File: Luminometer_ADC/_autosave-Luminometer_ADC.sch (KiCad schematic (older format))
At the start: 69 parts, among them J1 Harting__15210122401000, U1 LT3464, U2 ADA4522-1, U3 ADR512, U4 ADR512, U5 ADA4522-4, U6 LP5907MFX-3, U7 ADS131M08IPBS

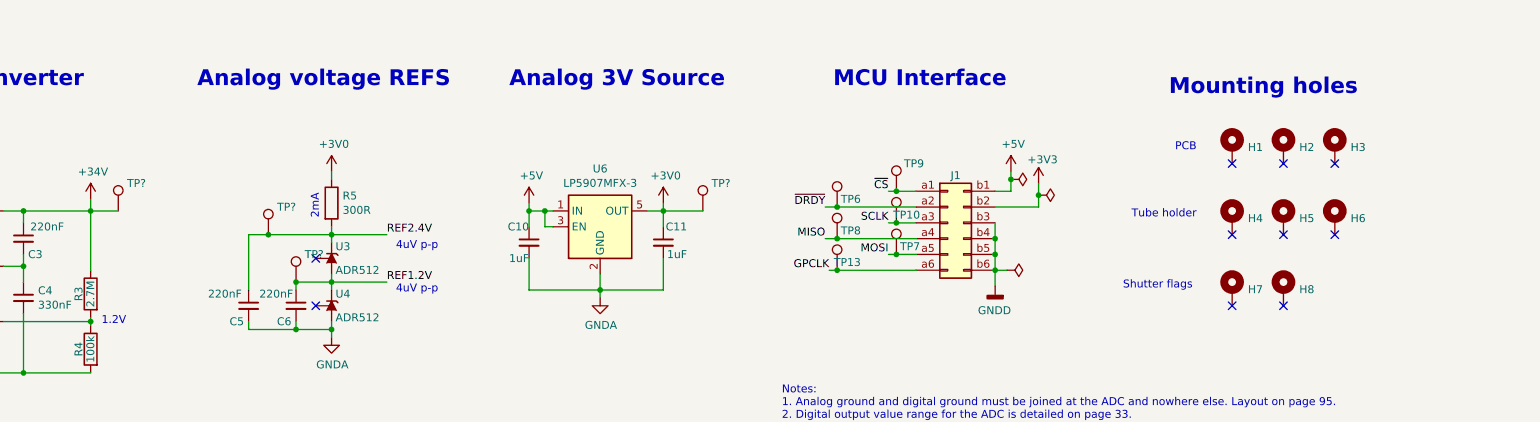
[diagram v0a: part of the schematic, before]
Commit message: Changes to design
- Standardized mounting hole pattern to match Pi zero.
- Rounded corners to 3 mm
- Moved all test points to back side of board.
- Added test points for +34V, 1.2V, 2.4V
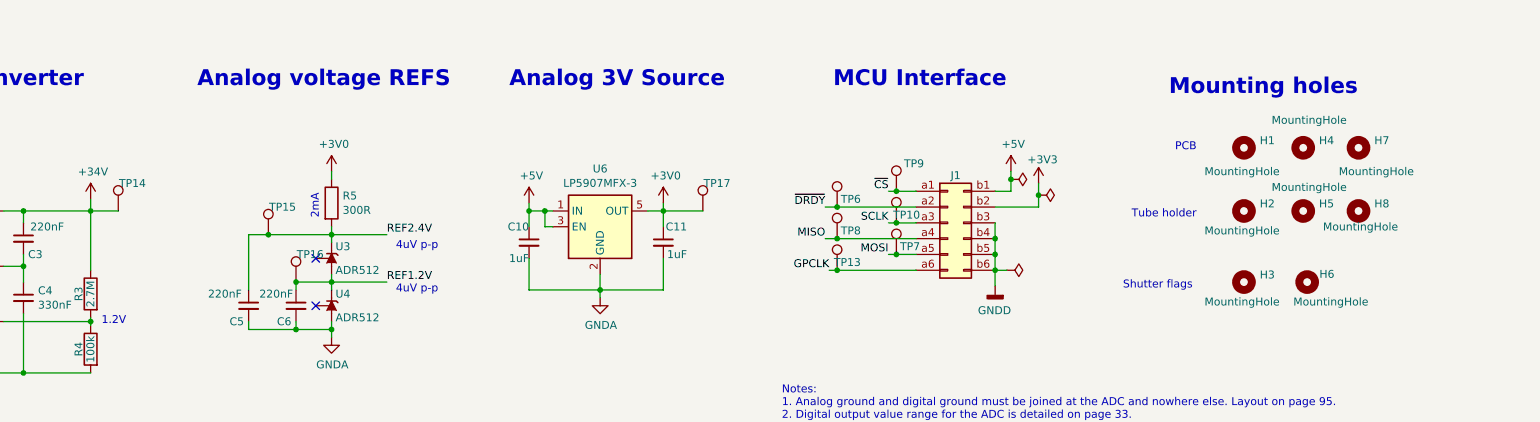
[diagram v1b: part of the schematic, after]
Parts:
- removed H1, H2, H3: MountingHole_Pad, MountingHole:MountingHole_2.7mm_M2.5_DIN965_Pad, symbol Mechanical:MountingHole_Pad
- removed H4, H5, H6: MountingHole_Pad, MountingHole:MountingHole_2.5mm, symbol Mechanical:MountingHole_Pad
- removed H7, H8: MountingHole_Pad, MountingHole:MountingHole_2.2mm_M2, symbol Mechanical:MountingHole_Pad
- added H1, H2, H4, H5, H7, H8: MountingHole, MountingHole:MountingHole_2.7mm_M2.5, symbol Mechanical:MountingHole
- added H3, H6: MountingHole, MountingHole:MountingHole_2.2mm_M2, symbol Mechanical:MountingHole
- gave numbers to parts that had none: 4
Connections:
- no-connect marks 13 -> 5
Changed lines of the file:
@@
 Connection ~ 10575 3050
-$Comp
-L Mechanical:MountingHole_Pad H1
-U 1 1 5F30D92E
-P 9850 5075
-F 0 "H1" H 9950 5078 50  0000 L CNN
-F 1 "MountingHole_Pad" H 9950 5033 50  0001 L CNN
-F 2 "MountingHole:MountingHole_2.7mm_M2.5_DIN965_Pad" H 9850 5075 50  0001 C CNN
-F 3 "~" H 9850 5075 50  0001 C CNN
-	1    9850 5075
-	1    0    0    -1
-$EndComp
 $Comp
 L LuminometerCustomPartLib:MICROFC−60035−SMT SiPM1
@@
 Wire Wire Line
 	3800 3325 3800 3375
-$Comp
-L Mechanical:MountingHole_Pad H2
-U 1 1 6163C291
-P 10175 5075
-F 0 "H2" H 10275 5078 50  0000 L CNN
-F 1 "MountingHole_Pad" H 10275 5033 50  0001 L CNN
-F 2 "MountingHole:MountingHole_2.7mm_M2.5_DIN965_Pad" H 10175 5075 50  0001 C CNN
-F 3 "~" H 10175 5075 50  0001 C CNN
-	1    10175 5075
-	1    0    0    -1
-$EndComp
-$Comp
-L Mechanical:MountingHole_Pad H3
-U 1 1 6163C601
-P 10500 5075
-F 0 "H3" H 10600 5078 50  0000 L CNN
-F 1 "MountingHole_Pad" H 10600 5033 50  0001 L CNN
-F 2 "MountingHole:MountingHole_2.7mm_M2.5_DIN965_Pad" H 10500 5075 50  0001 C CNN
-F 3 "~" H 10500 5075 50  0001 C CNN
-	1    10500 5075
-	1    0    0    -1
-$EndComp
-NoConn ~ 10500 5175
-NoConn ~ 10175 5175
-NoConn ~ 9850 5175
 Text Notes 5675 1900 0    39   ~ 0
 Precision
@@
 $EndComp
 Connection ~ 10575 3550
-$Comp
-L Mechanical:MountingHole_Pad H4
-U 1 1 616FF489
-P 9850 5525
-F 0 "H4" H 9950 5528 50  0000 L CNN
-F 1 "MountingHole_Pad" H 9950 5483 50  0001 L CNN
-F 2 "MountingHole:MountingHole_2.5mm" H 9850 5525 50  0001 C CNN
-F 3 "~" H 9850 5525 50  0001 C CNN
-	1    9850 5525
-	1    0    0    -1
-$EndComp
 Text Notes 9625 5100 2    50   ~ 0
 PCB
 Text Notes 9625 5525 2    50   ~ 0
 Tube holder
-$Comp
-L Mechanical:MountingHole_Pad H5
-U 1 1 61761F5F
-P 10175 5525
-F 0 "H5" H 10275 5528 50  0000 L CNN
-F 1 "MountingHole_Pad" H 10275 5483 50  0001 L CNN
-F 2 "MountingHole:MountingHole_2.5mm" H 10175 5525 50  0001 C CNN
-F 3 "~" H 10175 5525 50  0001 C CNN
-	1    10175 5525
-	1    0    0    -1
-$EndComp
-$Comp
-L Mechanical:MountingHole_Pad H6
-U 1 1 617622BC
-P 10500 5525
-F 0 "H6" H 10600 5528 50  0000 L CNN
-F 1 "MountingHole_Pad" H 10600 5483 50  0001 L CNN
-F 2 "MountingHole:MountingHole_2.5mm" H 10500 5525 50  0001 C CNN
-F 3 "~" H 10500 5525 50  0001 C CNN
-	1    10500 5525
-	1    0    0    -1
-$EndComp
-$Comp
-L Mechanical:MountingHole_Pad H7
-U 1 1 61762E6B
-P 9850 5975
-F 0 "H7" H 9950 5978 50  0000 L CNN
-F 1 "MountingHole_Pad" H 9950 5933 50  0001 L CNN
-F 2 "MountingHole:MountingHole_2.2mm_M2" H 9850 5975 50  0001 C CNN
-F 3 "~" H 9850 5975 50  0001 C CNN
-	1    9850 5975
-	1    0    0    -1
-$EndComp
-$Comp
-L Mechanical:MountingHole_Pad H8
-U 1 1 617631A2
-P 10175 5975
-F 0 "H8" H 10275 5978 50  0000 L CNN
-F 1 "MountingHole_Pad" H 10275 5933 50  0001 L CNN
-F 2 "MountingHole:MountingHole_2.2mm_M2" H 10175 5975 50  0001 C CNN
-F 3 "~" H 10175 5975 50  0001 C CNN
-	1    10175 5975
-	1    0    0    -1
-$EndComp
 Text Notes 9600 5975 2    50   ~ 0
 Shutter flags
@@
 Wire Wire Line
 	3625 5625 3750 5625
-NoConn ~ 9850 5625
-NoConn ~ 10175 5625
-NoConn ~ 10500 5625
-NoConn ~ 9850 6075
-NoConn ~ 10175 6075
-$Comp
-L Connector:TestPoint TP?
+$Comp
+L Connector:TestPoint TP17
 U 1 1 5FD30742
 P 6500 5475
-F 0 "TP?" H 6675 5650 50  0000 R CNN
+F 0 "TP17" H 6675 5650 50  0000 R CNN
 F 1 "TestPoint" H 6600 5675 50  0001 R CNN
 F 2 "TestPoint:TestPoint_Pad_D1.5mm" H 6700 5475 50  0001 C CNN
@@
 	6500 5475 6250 5475
 $Comp
-L Connector:TestPoint TP?
+L Connector:TestPoint TP15
 U 1 1 5FD40634
 P 3750 5625
-F 0 "TP?" H 3925 5800 50  0000 R CNN
+F 0 "TP15" H 3925 5800 50  0000 R CNN
 F 1 "TestPoint" H 3850 5825 50  0001 R CNN
 F 2 "TestPoint:TestPoint_Pad_D1.5mm" H 3950 5625 50  0001 C CNN
@@
 	3750 5625 4150 5625
 $Comp
-L Connector:TestPoint TP?
+L Connector:TestPoint TP16
 U 1 1 5FD40C16
 P 3925 5925
-F 0 "TP?" H 4100 6100 50  0000 R CNN
+F 0 "TP16" H 4100 6100 50  0000 R CNN
 F 1 "TestPoint" H 4025 6125 50  0001 R CNN
 F 2 "TestPoint:TestPoint_Pad_D1.5mm" H 4125 5925 50  0001 C CNN
@@
 Connection ~ 3925 5925
 $Comp
-L Connector:TestPoint TP?
+L Connector:TestPoint TP14
 U 1 1 5FD40E56
 P 2800 5475
-F 0 "TP?" H 2975 5650 50  0000 R CNN
+F 0 "TP14" H 2975 5650 50  0000 R CNN
 F 1 "TestPoint" H 2900 5675 50  0001 R CNN
 F 2 "TestPoint:TestPoint_Pad_D1.5mm" H 3000 5475 50  0001 C CNN
@@
 Wire Wire Line
 	2800 5475 2625 5475
+$Comp
+L Mechanical:MountingHole H3
+U 1 1 5FD63B89
+P 9925 5925
+F 0 "H3" H 10025 5971 50  0000 L CNN
+F 1 "MountingHole" H 9675 5800 50  0000 L CNN
+F 2 "MountingHole:MountingHole_2.2mm_M2" H 9925 5925 50  0001 C CNN
+F 3 "~" H 9925 5925 50  0001 C CNN
+	1    9925 5925
+	1    0    0    -1
+$EndComp
+$Comp
+L Mechanical:MountingHole H6
+U 1 1 5FDB2C55
+P 10325 5925
+F 0 "H6" H 10450 5975 50  0000 C CNN
+F 1 "MountingHole" H 10475 5800 50  0000 C CNN
+F 2 "MountingHole:MountingHole_2.2mm_M2" H 10325 5925 50  0001 C CNN
+F 3 "~" H 10325 5925 50  0001 C CNN
+	1    10325 5925
+	1    0    0    -1
+$EndComp
+$Comp
+L Mechanical:MountingHole H2
+U 1 1 5FD83D7B
+P 9925 5475
+F 0 "H2" H 10025 5521 50  0000 L CNN
+F 1 "MountingHole" H 9675 5350 50  0000 L CNN
+F 2 "MountingHole:MountingHole_2.7mm_M2.5" H 9925 5475 50  0001 C CNN
+F 3 "~" H 9925 5475 50  0001 C CNN
+	1    9925 5475
+	1    0    0    -1
+$EndComp
+$Comp
+L Mechanical:MountingHole H5
+U 1 1 5FD83D85
+P 10300 5475
+F 0 "H5" H 10400 5521 50  0000 L CNN
+F 1 "MountingHole" H 10100 5625 50  0000 L CNN
+F 2 "MountingHole:MountingHole_2.7mm_M2.5" H 10300 5475 50  0001 C CNN
+F 3 "~" H 10300 5475 50  0001 C CNN
+	1    10300 5475
+	1    0    0    -1
+$EndComp
+$Comp
+L Mechanical:MountingHole H8
+U 1 1 5FDB2488
+P 10650 5475
+F 0 "H8" H 10750 5521 50  0000 L CNN
+F 1 "MountingHole" H 10425 5375 50  0000 L CNN
+F 2 "MountingHole:MountingHole_2.7mm_M2.5" H 10650 5475 50  0001 C CNN
+F 3 "~" H 10650 5475 50  0001 C CNN
+	1    10650 5475
+	1    0    0    -1
+$EndComp
+$Comp
+L Mechanical:MountingHole H7
+U 1 1 5FD74442
+P 10650 5075
+F 0 "H7" H 10750 5121 50  0000 L CNN
+F 1 "MountingHole" H 10525 4925 50  0000 L CNN
+F 2 "MountingHole:MountingHole_2.7mm_M2.5" H 10650 5075 50  0001 C CNN
+F 3 "~" H 10650 5075 50  0001 C CNN
+	1    10650 5075
+	1    0    0    -1
+$EndComp
+$Comp
+L Mechanical:MountingHole H4
+U 1 1 5FD741C7
+P 10300 5075
+F 0 "H4" H 10400 5121 50  0000 L CNN
+F 1 "MountingHole" H 10100 5250 50  0000 L CNN
+F 2 "MountingHole:MountingHole_2.7mm_M2.5" H 10300 5075 50  0001 C CNN
+F 3 "~" H 10300 5075 50  0001 C CNN
+	1    10300 5075
+	1    0    0    -1
+$EndComp
+$Comp
+L Mechanical:MountingHole H1
+U 1 1 5FD6335D
+P 9925 5075
+F 0 "H1" H 10025 5121 50  0000 L CNN
+F 1 "MountingHole" H 9675 4925 50  0000 L CNN
+F 2 "MountingHole:MountingHole_2.7mm_M2.5" H 9925 5075 50  0001 C CNN
+F 3 "~" H 9925 5075 50  0001 C CNN
+	1    9925 5075
+	1    0    0    -1
+$EndComp
 $EndSCHEMATC
